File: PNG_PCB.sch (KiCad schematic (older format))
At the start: 1 part, among them U1 Teensy4.1

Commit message: copied teensy footprint over to PNG_PCB.pretty
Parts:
- U1: footprint teensy:Teensy41 -> PNG_PCB:Teensy41
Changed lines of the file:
@@
 F 0 "U1" H 8400 6365 50  0000 C CNN
 F 1 "Teensy4.1" H 8400 6274 50  0000 C CNN
-F 2 "teensy:Teensy41" H 8000 4200 50  0001 C CNN
+F 2 "PNG_PCB:Teensy41" H 8000 4200 50  0001 C CNN
 F 3 "" H 8000 4200 50  0001 C CNN
 	1    8400 3800

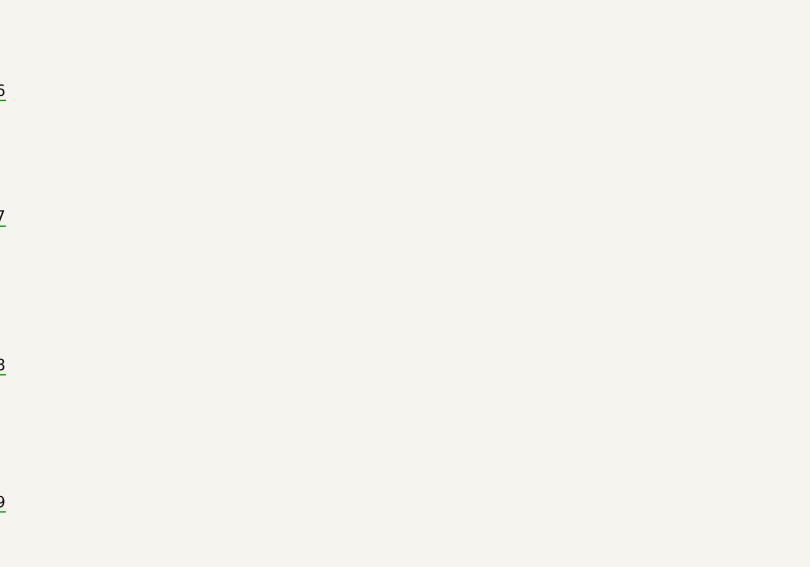
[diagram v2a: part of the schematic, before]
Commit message: added battery
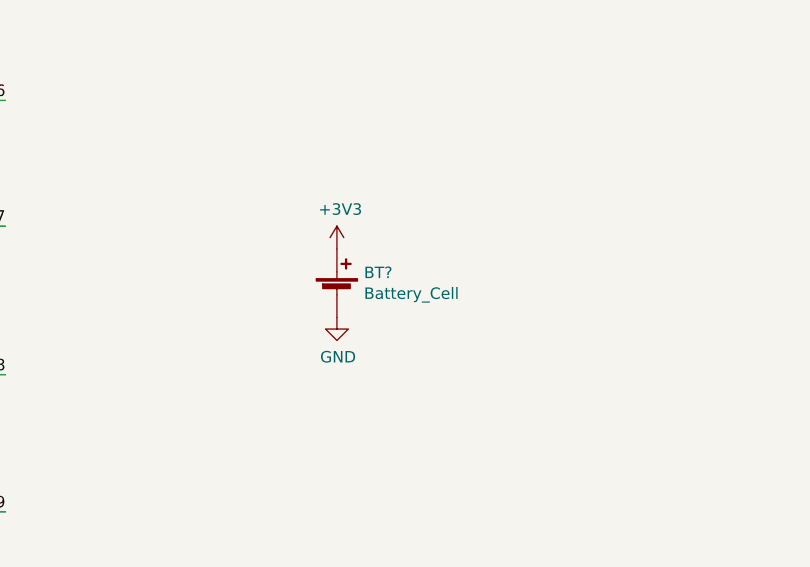
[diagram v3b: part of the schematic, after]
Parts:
- added BT?: Battery_Cell, Battery:BatteryHolder_Keystone_103_1x20mm, symbol Device:Battery_Cell
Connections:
- net +3V3: now also BT?.1 (+)
- net GND: now also BT?.2 (-)
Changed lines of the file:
@@
 NoConn ~ 7300 1750
 NoConn ~ 7300 3250
+$Comp
+L Device:Battery_Cell BT?
+U 1 1 60B5A3B5
+P 4700 5500
+F 0 "BT?" H 4818 5596 50  0000 L CNN
+F 1 "Battery_Cell" H 4818 5505 50  0000 L CNN
+F 2 "Battery:BatteryHolder_Keystone_103_1x20mm" V 4700 5560 50  0001 C CNN
+F 3 "~" V 4700 5560 50  0001 C CNN
+	1    4700 5500
+	1    0    0    -1
+$EndComp
+$Comp
+L power:GND #PWR?
+U 1 1 60B5A5A9
+P 4700 5600
+F 0 "#PWR?" H 4700 5350 50  0001 C CNN
+F 1 "GND" H 4705 5427 50  0000 C CNN
+F 2 "" H 4700 5600 50  0001 C CNN
+F 3 "" H 4700 5600 50  0001 C CNN
+	1    4700 5600
+	1    0    0    -1
+$EndComp
+$Comp
+L power:+3V3 #PWR?
+U 1 1 60B5A6A3
+P 4700 5300
+F 0 "#PWR?" H 4700 5150 50  0001 C CNN
+F 1 "+3V3" H 4715 5473 50  0000 C CNN
+F 2 "" H 4700 5300 50  0001 C CNN
+F 3 "" H 4700 5300 50  0001 C CNN
+	1    4700 5300
+	1    0    0    -1
+$EndComp
 $EndSCHEMATC

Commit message: left off with esp32 needing integration
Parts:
- added U10: ESP32-WROOM-32U, RF_Module:ESP32-WROOM-32U, symbol RF_Module:ESP32-WROOM-32U
- gave numbers to parts that had none: 1
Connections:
- new net: U10.1 (GND), U10.15 (GND), U10.38 (GND), U10.39 (GND)
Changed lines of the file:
@@
 NoConn ~ 7300 3250
 $Comp
-L Device:Battery_Cell BT?
+L Device:Battery_Cell BT1
 U 1 1 60B5A3B5
 P 4700 5500
-F 0 "BT?" H 4818 5596 50  0000 L CNN
+F 0 "BT1" H 4818 5596 50  0000 L CNN
 F 1 "Battery_Cell" H 4818 5505 50  0000 L CNN
 F 2 "Battery:BatteryHolder_Keystone_103_1x20mm" V 4700 5560 50  0001 C CNN
@@
 $EndComp
 $Comp
-L power:GND #PWR?
+L power:GND #PWR0101
 U 1 1 60B5A5A9
 P 4700 5600
-F 0 "#PWR?" H 4700 5350 50  0001 C CNN
+F 0 "#PWR0101" H 4700 5350 50  0001 C CNN
 F 1 "GND" H 4705 5427 50  0000 C CNN
 F 2 "" H 4700 5600 50  0001 C CNN
@@
 $EndComp
 $Comp
-L power:+3V3 #PWR?
+L power:+3V3 #PWR0102
 U 1 1 60B5A6A3
 P 4700 5300
-F 0 "#PWR?" H 4700 5150 50  0001 C CNN
+F 0 "#PWR0102" H 4700 5150 50  0001 C CNN
 F 1 "+3V3" H 4715 5473 50  0000 C CNN
 F 2 "" H 4700 5300 50  0001 C CNN
@@
 	1    0    0    -1
 $EndComp
+$Comp
+L RF_Module:ESP32-WROOM-32U U10
+U 1 1 60B5E875
+P 4800 2550
+F 0 "U10" H 4800 4131 50  0000 C CNN
+F 1 "ESP32-WROOM-32U" H 4800 4040 50  0000 C CNN
+F 2 "RF_Module:ESP32-WROOM-32U" H 4800 1050 50  0001 C CNN
+F 3 "https://www.espressif.com/sites/default/files/documentation/esp32-wroom-32d_esp32-wroom-32u_datasheet_en.pdf" H 4500 2600 50  0001 C CNN
+	1    4800 2550
+	1    0    0    -1
+$EndComp
